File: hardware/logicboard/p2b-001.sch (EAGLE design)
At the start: 70 parts, among them IC1 74LS06N, IC2 4066N, J1 MKR, J2 GPIO, J3 Vcc, J4 3-PIN SMD, J42 RLY2, J5 SPI, J6 LED, J7 DIN5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

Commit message: Silk.
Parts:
- removed J4: 3-PIN SMD, SparkFun-Connectors:CONN_03JST-SMD
- added RZ3***, RZ4***: Inf, rcl:R-EU_M2012
- renumbered J42 to J4***
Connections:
- new net RLYOUT1: J4***.2, RZ3***.2
- new net RLYOUT2: J4***.3, RZ4***.2
- net RLYOUT: no longer J4.1
- net VOUTRAW: now also RZ3***.1; no longer J4***.2, J4.2
- net VOUTRAW2: now also RZ4***.1; no longer J4***.3, J4.3
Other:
- moved on the sheet: F1
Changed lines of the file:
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@@
 <part name="VCCBRIDGE**" library="rcl" library_urn="urn:adsk.eagle:library:334" deviceset="R-EU_" device="M2012" package3d_urn="urn:adsk.eagle:package:23561/2" value="Inf"/>
 <part name="SUPPLY25" library="supply2" library_urn="urn:adsk.eagle:library:372" deviceset="VCC" device=""/>
-<part name="J42" library="SparkFun-Connectors" library_urn="urn:adsk.eagle:library:513" deviceset="CONN_03" device="JST-PTH" package3d_urn="urn:adsk.eagle:package:38069/1" value="RLY2"/>
-<part name="J4" library="SparkFun-Connectors" library_urn="urn:adsk.eagle:library:513" deviceset="CONN_03" device="JST-SMD" package3d_urn="urn:adsk.eagle:package:38075/1" value="3-PIN SMD"/>
+<part name="J4***" library="SparkFun-Connectors" library_urn="urn:adsk.eagle:library:513" deviceset="CONN_03" device="JST-PTH" package3d_urn="urn:adsk.eagle:package:38069/1" value="RLY2"/>
+<part name="RZ4***" library="rcl" library_urn="urn:adsk.eagle:library:334" deviceset="R-EU_" device="M2012" package3d_urn="urn:adsk.eagle:package:23561/2" value="Inf"/>
+<part name="RZ3***" library="rcl" library_urn="urn:adsk.eagle:library:334" deviceset="R-EU_" device="M2012" package3d_urn="urn:adsk.eagle:package:23561/2" value="Inf"/>
 </parts>
 <sheets>
@@
 </instance>
 <instance part="SUPPLY23" gate="GND" x="60.96" y="81.28" smashed="yes"/>
-<instance part="F1" gate="1" x="114.3" y="218.44" smashed="yes" rot="R90">
-<attribute name="NAME" x="111.76" y="218.44" size="1.778" layer="95" rot="R90" align="bottom-center"/>
-<attribute name="VALUE" x="116.84" y="218.44" size="1.778" layer="96" rot="R90" align="bottom-center"/>
+<instance part="F1" gate="1" x="114.3" y="223.52" smashed="yes" rot="R90">
+<attribute name="NAME" x="111.76" y="223.52" size="1.778" layer="95" rot="R90" align="bottom-center"/>
+<attribute name="VALUE" x="116.84" y="223.52" size="1.778" layer="96" rot="R90" align="bottom-center"/>
 </instance>
 <instance part="R3" gate="G$1" x="205.74" y="157.48" smashed="yes" rot="R90">
@@
 <attribute name="VALUE" x="312.42" y="119.38" size="1.778" layer="96" align="bottom-center"/>
 </instance>
-<instance part="J42" gate="J$1" x="111.76" y="50.8" smashed="yes">
+<instance part="J4***" gate="J$1" x="111.76" y="50.8" smashed="yes">
 <attribute name="VALUE" x="111.76" y="43.18" size="1.778" layer="96" align="bottom-center"/>
 <attribute name="NAME" x="111.76" y="55.88" size="1.778" layer="95" align="bottom-center"/>
 </instance>
-<instance part="J4" gate="J$1" x="88.9" y="50.8" smashed="yes">
-<attribute name="VALUE" x="86.36" y="43.434" size="1.778" layer="96" font="vector"/>
-<attribute name="NAME" x="86.36" y="56.388" size="1.778" layer="95" font="vector"/>
+<instance part="RZ4***" gate="G$1" x="124.46" y="220.98" smashed="yes" rot="R90">
+<attribute name="NAME" x="122.9614" y="217.17" size="1.778" layer="95" rot="R90"/>
+<attribute name="VALUE" x="127.762" y="217.17" size="1.778" layer="96" rot="R90"/>
+</instance>
+<instance part="RZ3***" gate="G$1" x="137.16" y="220.98" smashed="yes" rot="R90">
+<attribute name="NAME" x="135.6614" y="217.17" size="1.778" layer="95" rot="R90"/>
+<attribute name="VALUE" x="140.462" y="217.17" size="1.778" layer="96" rot="R90"/>
 </instance>
 </instances>
@@
 <segment>
 <pinref part="F1" gate="1" pin="1"/>
+<wire x1="114.3" y1="218.44" x2="114.3" y2="213.36" width="0.1524" layer="91"/>
+<pinref part="K1" gate="2" pin="O"/>
 <wire x1="114.3" y1="213.36" x2="114.3" y2="210.82" width="0.1524" layer="91"/>
-<pinref part="K1" gate="2" pin="O"/>
 <wire x1="114.3" y1="210.82" x2="116.84" y2="210.82" width="0.1524" layer="91"/>
 <pinref part="JP4" gate="G$1" pin="1"/>
@@
 <junction x="104.14" y="210.82"/>
 <label x="104.14" y="210.82" size="1.778" layer="95"/>
-</segment>
-<segment>
-<wire x1="121.92" y1="53.34" x2="119.38" y2="53.34" width="0.1524" layer="91"/>
-<label x="121.92" y="53.34" size="0.8128" layer="95" xref="yes"/>
-<pinref part="J42" gate="J$1" pin="3"/>
-</segment>
-<segment>
-<pinref part="J4" gate="J$1" pin="3"/>
+<pinref part="RZ4***" gate="G$1" pin="1"/>
+<wire x1="124.46" y1="215.9" x2="124.46" y2="213.36" width="0.1524" layer="91"/>
+<wire x1="124.46" y1="213.36" x2="114.3" y2="213.36" width="0.1524" layer="91"/>
+<junction x="114.3" y="213.36"/>
+</segment>
+<segment>
 <wire x1="96.52" y1="53.34" x2="99.06" y2="53.34" width="0.1524" layer="91"/>
 <label x="99.06" y="53.34" size="0.8128" layer="95" xref="yes"/>
@@
 <label x="116.84" y="233.68" size="0.8128" layer="95" xref="yes"/>
 <wire x1="114.3" y1="233.68" x2="116.84" y2="233.68" width="0.1524" layer="91"/>
-<wire x1="114.3" y1="223.52" x2="114.3" y2="231.14" width="0.1524" layer="91"/>
+<wire x1="114.3" y1="228.6" x2="114.3" y2="231.14" width="0.1524" layer="91"/>
 <junction x="114.3" y="233.68"/>
 <wire x1="114.3" y1="231.14" x2="114.3" y2="233.68" width="0.1524" layer="91"/>
@@
 <wire x1="124.46" y1="200.66" x2="132.08" y2="200.66" width="0.1524" layer="91"/>
 <junction x="124.46" y="200.66"/>
-<wire x1="132.08" y1="200.66" x2="132.08" y2="220.98" width="0.1524" layer="91"/>
+<wire x1="132.08" y1="200.66" x2="132.08" y2="213.36" width="0.1524" layer="91"/>
 <label x="132.08" y="220.98" size="0.8128" layer="95" rot="R90" xref="yes"/>
 <pinref part="B" gate="1" pin="P"/>
+<wire x1="132.08" y1="213.36" x2="132.08" y2="220.98" width="0.1524" layer="91"/>
 <wire x1="106.68" y1="215.9" x2="106.68" y2="208.28" width="0.1524" layer="91"/>
 <junction x="106.68" y="208.28"/>
+<pinref part="RZ3***" gate="G$1" pin="1"/>
+<wire x1="137.16" y1="213.36" x2="137.16" y2="215.9" width="0.1524" layer="91"/>
+<wire x1="137.16" y1="213.36" x2="132.08" y2="213.36" width="0.1524" layer="91"/>
+<junction x="132.08" y="213.36"/>
 </segment>
 <segment>
 <wire x1="96.52" y1="50.8" x2="99.06" y2="50.8" width="0.1524" layer="91"/>
 <label x="99.06" y="50.8" size="0.8128" layer="95" xref="yes"/>
-<pinref part="J4" gate="J$1" pin="2"/>
-</segment>
-<segment>
-<wire x1="119.38" y1="50.8" x2="121.92" y2="50.8" width="0.1524" layer="91"/>
-<label x="121.92" y="50.8" size="0.8128" layer="95" xref="yes"/>
-<pinref part="J42" gate="J$1" pin="2"/>
 </segment>
 </net>
@@
 <pinref part="K1" gate="2" pin="S"/>
 <wire x1="127" y1="210.82" x2="129.54" y2="210.82" width="0.1524" layer="91"/>
+<label x="129.54" y="220.98" size="0.8128" layer="95" rot="R90" xref="yes"/>
 <wire x1="129.54" y1="210.82" x2="129.54" y2="220.98" width="0.1524" layer="91"/>
-<label x="129.54" y="220.98" size="0.8128" layer="95" rot="R90" xref="yes"/>
 </segment>
 <segment>
 <wire x1="96.52" y1="48.26" x2="99.06" y2="48.26" width="0.1524" layer="91"/>
 <label x="99.06" y="48.26" size="0.8128" layer="95" xref="yes"/>
-<pinref part="J4" gate="J$1" pin="1"/>
 </segment>
 <segment>
 <wire x1="119.38" y1="48.26" x2="121.92" y2="48.26" width="0.1524" layer="91"/>
 <label x="121.92" y="48.26" size="0.8128" layer="95" xref="yes"/>
-<pinref part="J42" gate="J$1" pin="1"/>
+<pinref part="J4***" gate="J$1" pin="1"/>
 </segment>
 </net>
@@
 </segment>
 </net>
+<net name="RLYOUT2" class="0">
+<segment>
+<pinref part="RZ4***" gate="G$1" pin="2"/>
+<wire x1="124.46" y1="226.06" x2="124.46" y2="228.6" width="0.1524" layer="91"/>
+<label x="124.46" y="228.6" size="0.8128" layer="95" rot="R90" xref="yes"/>
+</segment>
+<segment>
+<wire x1="121.92" y1="53.34" x2="119.38" y2="53.34" width="0.1524" layer="91"/>
+<label x="121.92" y="53.34" size="0.8128" layer="95" xref="yes"/>
+<pinref part="J4***" gate="J$1" pin="3"/>
+</segment>
+</net>
+<net name="RLYOUT1" class="0">
+<segment>
+<pinref part="RZ3***" gate="G$1" pin="2"/>
+<wire x1="137.16" y1="226.06" x2="137.16" y2="228.6" width="0.1524" layer="91"/>
+<label x="137.16" y="228.6" size="0.8128" layer="95" rot="R90" xref="yes"/>
+</segment>
+<segment>
+<wire x1="119.38" y1="50.8" x2="121.92" y2="50.8" width="0.1524" layer="91"/>
+<label x="121.92" y="50.8" size="0.8128" layer="95" xref="yes"/>
+<pinref part="J4***" gate="J$1" pin="2"/>
+</segment>
+</net>

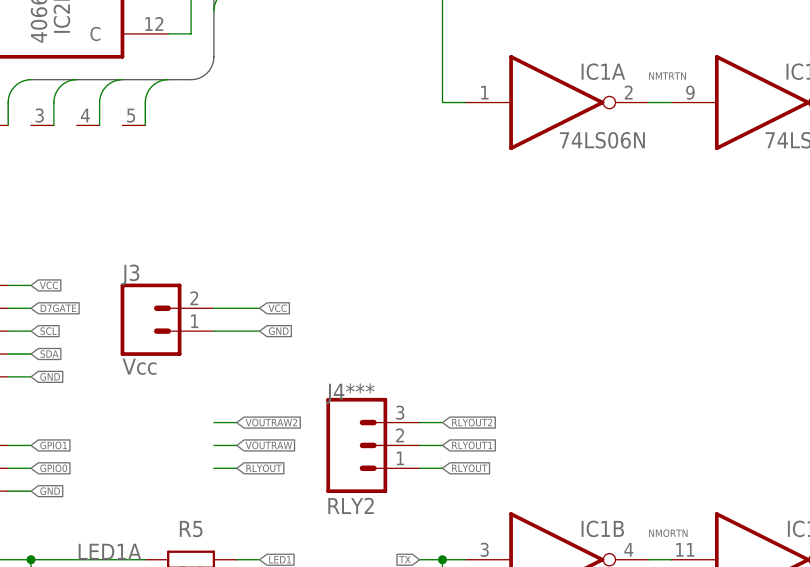
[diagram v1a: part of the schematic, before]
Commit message: Reset pins.
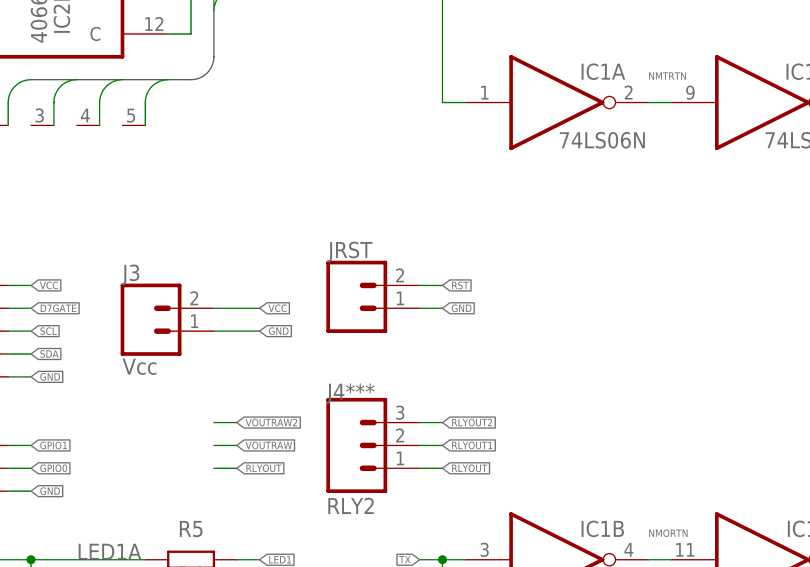
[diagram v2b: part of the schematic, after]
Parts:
- added JRST: (no value), SparkFun-Connectors:CONN_02
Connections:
- net GND: now also JRST.1
- net RST: now also JRST.2
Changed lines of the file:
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@@
 <part name="RZ4***" library="rcl" library_urn="urn:adsk.eagle:library:334" deviceset="R-EU_" device="M2012" package3d_urn="urn:adsk.eagle:package:23561/2" value="Inf"/>
 <part name="RZ3***" library="rcl" library_urn="urn:adsk.eagle:library:334" deviceset="R-EU_" device="M2012" package3d_urn="urn:adsk.eagle:package:23561/2" value="Inf"/>
+<part name="JRST" library="SparkFun-Connectors" library_urn="urn:adsk.eagle:library:513" deviceset="CONN_02" device="" package3d_urn="urn:adsk.eagle:package:38039/1"/>
 </parts>
 <sheets>
@@
 <attribute name="NAME" x="135.6614" y="217.17" size="1.778" layer="95" rot="R90"/>
 <attribute name="VALUE" x="140.462" y="217.17" size="1.778" layer="96" rot="R90"/>
+</instance>
+<instance part="JRST" gate="G$1" x="111.76" y="66.04" smashed="yes">
+<attribute name="VALUE" x="109.22" y="61.214" size="1.778" layer="96" font="vector"/>
+<attribute name="NAME" x="109.22" y="71.628" size="1.778" layer="95" font="vector"/>
 </instance>
 </instances>
@@
 <pinref part="SUPPLY21" gate="GND" pin="GND"/>
 </segment>
+<segment>
+<pinref part="JRST" gate="G$1" pin="1"/>
+<wire x1="119.38" y1="66.04" x2="121.92" y2="66.04" width="0.1524" layer="91"/>
+<label x="121.92" y="66.04" size="0.8128" layer="95" xref="yes"/>
+</segment>
 </net>
 <net name="VCC" class="2">
@@
 <label x="340.36" y="116.84" size="0.8128" layer="95" rot="MR0" xref="yes"/>
 </segment>
+<segment>
+<pinref part="JRST" gate="G$1" pin="2"/>
+<wire x1="119.38" y1="68.58" x2="121.92" y2="68.58" width="0.1524" layer="91"/>
+<label x="121.92" y="68.58" size="0.8128" layer="95" xref="yes"/>
+</segment>
 </net>

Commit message: SPI port. GPIO port. Vcc port.
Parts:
- removed JRST: (no value), SparkFun-Connectors:CONN_02
- J2: value GPIO -> (none); device SparkFun-Connectors:CONN_03JST-PTH -> SparkFun-Connectors:CONN_04JST-PTH
- J5: value SPI -> (none); device SparkFun-Connectors:CONN_05JST-VERT -> SparkFun-Connectors:CONN_061.27MM
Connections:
- net GND: now also J5.6; no longer J5.1, JRST.1
- net GPIO0: now also J2.3; no longer J2.2
- net GPIO1: now also J2.4; no longer J2.3
- net MISO: now also J5.1; no longer J5.5
- net RST: now also J5.5; no longer JRST.2
- net VCC: now also J2.2
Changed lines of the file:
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@@
 <part name="JP2" library="SparkFun-Connectors" library_urn="urn:adsk.eagle:library:513" deviceset="CONN_05" device="" package3d_urn="urn:adsk.eagle:package:38104/1" value="RTC"/>
 <part name="D1" library="SparkFun-DiscreteSemi" library_urn="urn:adsk.eagle:library:514" deviceset="DIODE" device="-1N4148" package3d_urn="urn:adsk.eagle:package:38452/1" value=""/>
-<part name="J2" library="SparkFun-Connectors" library_urn="urn:adsk.eagle:library:513" deviceset="CONN_03" device="JST-PTH" package3d_urn="urn:adsk.eagle:package:38069/1" value="GPIO"/>
 <part name="SUPPLY4" library="supply2" deviceset="GND" device=""/>
 <part name="X9" library="wirepad" library_urn="urn:adsk.eagle:library:412" deviceset="PAD-N" device=""/>
@@
 <part name="JP1" library="pinhead" library_urn="urn:adsk.eagle:library:325" deviceset="PINHD-2X3" device="" package3d_urn="urn:adsk.eagle:package:22462/2" value="PWRSEL"/>
 <part name="J3" library="SparkFun-Connectors" library_urn="urn:adsk.eagle:library:513" deviceset="CONN_02" device="JST-PTH-2" package3d_urn="urn:adsk.eagle:package:38053/1" value="Vcc"/>
-<part name="J5" library="SparkFun-Connectors" library_urn="urn:adsk.eagle:library:513" deviceset="CONN_05" device="JST-VERT" package3d_urn="urn:adsk.eagle:package:38111/1" value="SPI"/>
 <part name="RN4" library="resistor-dil" library_urn="urn:adsk.eagle:library:342" deviceset="8R-N" device="" package3d_urn="urn:adsk.eagle:package:922/2" value="220"/>
 <part name="RN3" library="resistor-net" library_urn="urn:adsk.eagle:library:343" deviceset="RN04" device="" package3d_urn="urn:adsk.eagle:package:24976/1" value="4.7k"/>
@@
 <part name="RZ4***" library="rcl" library_urn="urn:adsk.eagle:library:334" deviceset="R-EU_" device="M2012" package3d_urn="urn:adsk.eagle:package:23561/2" value="Inf"/>
 <part name="RZ3***" library="rcl" library_urn="urn:adsk.eagle:library:334" deviceset="R-EU_" device="M2012" package3d_urn="urn:adsk.eagle:package:23561/2" value="Inf"/>
-<part name="JRST" library="SparkFun-Connectors" library_urn="urn:adsk.eagle:library:513" deviceset="CONN_02" device="" package3d_urn="urn:adsk.eagle:package:38039/1"/>
+<part name="J2" library="SparkFun-Connectors" library_urn="urn:adsk.eagle:library:513" deviceset="CONN_04" device="JST-PTH" package3d_urn="urn:adsk.eagle:package:38101/1"/>
+<part name="J5" library="SparkFun-Connectors" library_urn="urn:adsk.eagle:library:513" deviceset="CONN_06" device="1.27MM" package3d_urn="urn:adsk.eagle:package:38131/1"/>
 </parts>
 <sheets>
@@
 <attribute name="VALUE" x="83.82" y="207.772" size="1.778" layer="96" font="vector" rot="R180" align="top-left"/>
 </instance>
-<instance part="J2" gate="J$1" x="66.04" y="48.26" smashed="yes">
-<attribute name="VALUE" x="60.96" y="48.26" size="1.778" layer="96" rot="R90" align="bottom-center"/>
-<attribute name="NAME" x="58.42" y="48.26" size="1.778" layer="95" rot="R90" align="bottom-center"/>
-</instance>
 <instance part="SUPPLY4" gate="GND" x="231.14" y="198.12" smashed="yes"/>
 <instance part="X9" gate="G$1" x="342.9" y="124.46" smashed="yes"/>
@@
 <attribute name="NAME" x="86.36" y="69.088" size="1.778" layer="95" font="vector"/>
 </instance>
-<instance part="J5" gate="G$1" x="88.9" y="17.78" smashed="yes">
-<attribute name="VALUE" x="86.36" y="7.874" size="1.778" layer="96" font="vector"/>
-<attribute name="NAME" x="86.36" y="25.908" size="1.778" layer="95" font="vector"/>
-</instance>
 <instance part="RN4" gate="A" x="205.74" y="114.3" smashed="yes" rot="R270">
 <attribute name="VALUE" x="202.692" y="111.76" size="1.778" layer="96" rot="R270"/>
@@
 <attribute name="VALUE" x="140.462" y="217.17" size="1.778" layer="96" rot="R90"/>
 </instance>
-<instance part="JRST" gate="G$1" x="111.76" y="66.04" smashed="yes">
-<attribute name="VALUE" x="109.22" y="61.214" size="1.778" layer="96" font="vector"/>
-<attribute name="NAME" x="109.22" y="71.628" size="1.778" layer="95" font="vector"/>
+<instance part="J2" gate="G$1" x="55.88" y="48.26" smashed="yes">
+<attribute name="VALUE" x="50.8" y="40.894" size="1.778" layer="96" font="vector"/>
+<attribute name="NAME" x="50.8" y="56.388" size="1.778" layer="95" font="vector"/>
+</instance>
+<instance part="J5" gate="G$1" x="91.44" y="15.24" smashed="yes">
+<attribute name="VALUE" x="86.36" y="5.334" size="1.778" layer="96" font="vector"/>
+<attribute name="NAME" x="86.36" y="25.908" size="1.778" layer="95" font="vector"/>
 </instance>
 </instances>
@@
 </segment>
 <segment>
-<pinref part="J2" gate="J$1" pin="1"/>
-<wire x1="73.66" y1="45.72" x2="76.2" y2="45.72" width="0.1524" layer="91"/>
 <label x="76.2" y="45.72" size="0.8128" layer="95" xref="yes"/>
+<pinref part="J2" gate="G$1" pin="1"/>
+<wire x1="76.2" y1="45.72" x2="60.96" y2="45.72" width="0.1524" layer="91"/>
 </segment>
 <segment>
@@
 </segment>
 <segment>
-<pinref part="J5" gate="G$1" pin="1"/>
-<wire x1="96.52" y1="12.7" x2="99.06" y2="12.7" width="0.1524" layer="91"/>
-<label x="99.06" y="12.7" size="0.8128" layer="95" xref="yes"/>
-</segment>
-<segment>
 <pinref part="OK1" gate="B" pin="C2"/>
 <wire x1="208.28" y1="101.6" x2="205.74" y2="101.6" width="0.1524" layer="91"/>
@@
 </segment>
 <segment>
-<pinref part="JRST" gate="G$1" pin="1"/>
-<wire x1="119.38" y1="66.04" x2="121.92" y2="66.04" width="0.1524" layer="91"/>
-<label x="121.92" y="66.04" size="0.8128" layer="95" xref="yes"/>
+<wire x1="96.52" y1="22.86" x2="99.06" y2="22.86" width="0.1524" layer="91"/>
+<label x="99.06" y="22.86" size="0.8128" layer="95" xref="yes"/>
+<pinref part="J5" gate="G$1" pin="6"/>
 </segment>
 </net>
@@
 </segment>
 <segment>
-<pinref part="J5" gate="G$1" pin="2"/>
-<wire x1="96.52" y1="15.24" x2="99.06" y2="15.24" width="0.1524" layer="91"/>
-<label x="99.06" y="15.24" size="0.8128" layer="95" xref="yes"/>
-</segment>
-<segment>
 <wire x1="96.52" y1="66.04" x2="101.6" y2="66.04" width="0.1524" layer="91"/>
 <pinref part="J3" gate="G$1" pin="2"/>
@@
 <pinref part="SUPPLY25" gate="G$1" pin="VCC"/>
 <wire x1="312.42" y1="109.22" x2="312.42" y2="111.76" width="0.1524" layer="91"/>
+</segment>
+<segment>
+<pinref part="J2" gate="G$1" pin="2"/>
+<wire x1="60.96" y1="48.26" x2="76.2" y2="48.26" width="0.1524" layer="91"/>
+<label x="76.2" y="48.26" size="0.8128" layer="95" xref="yes"/>
+</segment>
+<segment>
+<wire x1="96.52" y1="12.7" x2="99.06" y2="12.7" width="0.1524" layer="91"/>
+<label x="99.06" y="12.7" size="0.8128" layer="95" xref="yes"/>
+<pinref part="J5" gate="G$1" pin="2"/>
 </segment>
 </net>
@@
 </segment>
 <segment>
-<pinref part="JRST" gate="G$1" pin="2"/>
-<wire x1="119.38" y1="68.58" x2="121.92" y2="68.58" width="0.1524" layer="91"/>
-<label x="121.92" y="68.58" size="0.8128" layer="95" xref="yes"/>
+<wire x1="96.52" y1="20.32" x2="99.06" y2="20.32" width="0.1524" layer="91"/>
+<label x="99.06" y="20.32" size="0.8128" layer="95" xref="yes"/>
+<pinref part="J5" gate="G$1" pin="5"/>
 </segment>
 </net>
@@
 </segment>
 <segment>
-<pinref part="J2" gate="J$1" pin="3"/>
-<wire x1="73.66" y1="50.8" x2="76.2" y2="50.8" width="0.1524" layer="91"/>
-<label x="76.2" y="50.8" size="0.8128" layer="95" xref="yes"/>
+<wire x1="60.96" y1="53.34" x2="76.2" y2="53.34" width="0.1524" layer="91"/>
+<label x="76.2" y="53.34" size="0.8128" layer="95" xref="yes"/>
+<pinref part="J2" gate="G$1" pin="4"/>
 </segment>
 <segment>
@@
 </segment>
 <segment>
-<pinref part="J2" gate="J$1" pin="2"/>
-<wire x1="73.66" y1="48.26" x2="76.2" y2="48.26" width="0.1524" layer="91"/>
-<label x="76.2" y="48.26" size="0.8128" layer="95" xref="yes"/>
+<wire x1="60.96" y1="50.8" x2="76.2" y2="50.8" width="0.1524" layer="91"/>
+<label x="76.2" y="50.8" size="0.8128" layer="95" xref="yes"/>
+<pinref part="J2" gate="G$1" pin="3"/>
 </segment>
 <segment>
@@
 <wire x1="124.46" y1="213.36" x2="114.3" y2="213.36" width="0.1524" layer="91"/>
 <junction x="114.3" y="213.36"/>
-</segment>
-<segment>
-<wire x1="96.52" y1="53.34" x2="99.06" y2="53.34" width="0.1524" layer="91"/>
-<label x="99.06" y="53.34" size="0.8128" layer="95" xref="yes"/>
 </segment>
 </net>
@@
 <junction x="132.08" y="213.36"/>
 </segment>
-<segment>
-<wire x1="96.52" y1="50.8" x2="99.06" y2="50.8" width="0.1524" layer="91"/>
-<label x="99.06" y="50.8" size="0.8128" layer="95" xref="yes"/>
-</segment>
 </net>
 <net name="RLYOUT" class="0">
@@
 <label x="129.54" y="220.98" size="0.8128" layer="95" rot="R90" xref="yes"/>
 <wire x1="129.54" y1="210.82" x2="129.54" y2="220.98" width="0.1524" layer="91"/>
-</segment>
-<segment>
-<wire x1="96.52" y1="48.26" x2="99.06" y2="48.26" width="0.1524" layer="91"/>
-<label x="99.06" y="48.26" size="0.8128" layer="95" xref="yes"/>
 </segment>
 <segment>
@@
 </segment>
 <segment>
-<pinref part="J5" gate="G$1" pin="5"/>
-<wire x1="96.52" y1="22.86" x2="99.06" y2="22.86" width="0.1524" layer="91"/>
-<label x="99.06" y="22.86" size="0.8128" layer="95" xref="yes"/>
+<pinref part="J5" gate="G$1" pin="1"/>
+<wire x1="96.52" y1="10.16" x2="99.06" y2="10.16" width="0.1524" layer="91"/>
+<label x="99.06" y="10.16" size="0.8128" layer="95" xref="yes"/>
 </segment>
 </net>
@@
 </segment>
 <segment>
+<wire x1="96.52" y1="15.24" x2="99.06" y2="15.24" width="0.1524" layer="91"/>
+<label x="99.06" y="15.24" size="0.8128" layer="95" xref="yes"/>
 <pinref part="J5" gate="G$1" pin="3"/>
-<wire x1="96.52" y1="17.78" x2="99.06" y2="17.78" width="0.1524" layer="91"/>
-<label x="99.06" y="17.78" size="0.8128" layer="95" xref="yes"/>
 </segment>
 </net>
@@
 </segment>
 <segment>
+<wire x1="96.52" y1="17.78" x2="99.06" y2="17.78" width="0.1524" layer="91"/>
+<label x="99.06" y="17.78" size="0.8128" layer="95" xref="yes"/>
 <pinref part="J5" gate="G$1" pin="4"/>
-<wire x1="96.52" y1="20.32" x2="99.06" y2="20.32" width="0.1524" layer="91"/>
-<label x="99.06" y="20.32" size="0.8128" layer="95" xref="yes"/>
-</segment>
-</net>
+</segment>
+</net>
